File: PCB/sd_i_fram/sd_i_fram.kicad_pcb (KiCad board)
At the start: 2 copper layers, 50 x 40 mm, 11 parts, among them J1 Conn_02x05, J2 Micro_SD_Card

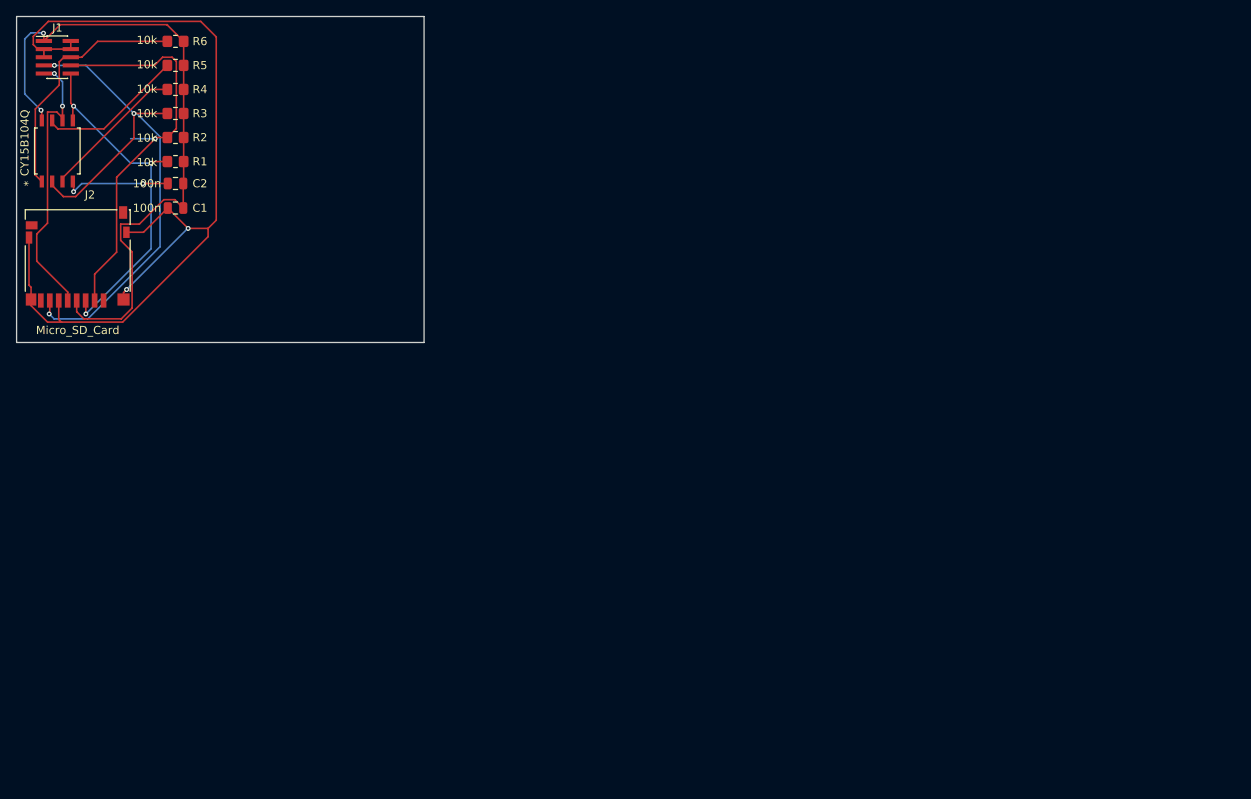
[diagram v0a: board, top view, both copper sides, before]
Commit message: poprawki po 'pracy' michala na schemacie. Poprawione PCB pamieci po Kubie. Grubsze sciezki, poprawiona pozycja decoupling capacitora
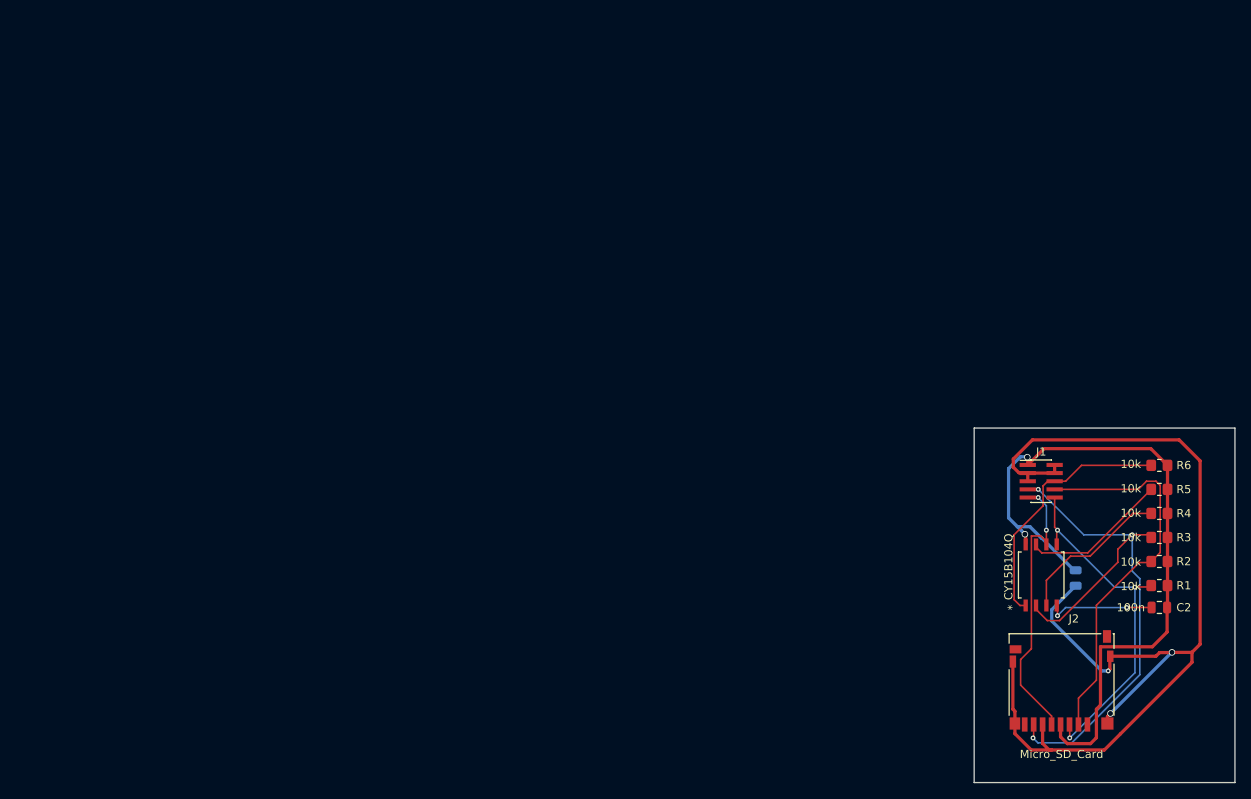
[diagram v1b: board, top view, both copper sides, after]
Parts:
- C1: moved to B.Cu
- moved C2 131.5 mm to (140.2, 72.5)
- moved FRAM1 131.5 mm to (125.7, 68.5)
- moved J1 131.5 mm to (125.7, 57.0)
- moved J2 131.5 mm to (128.2, 81.5)
- moved R1 131.5 mm to (140.2, 69.8)
- moved R2 131.5 mm to (140.2, 66.9)
- moved R3 131.5 mm to (140.2, 63.9)
- moved R4 131.5 mm to (140.2, 61.0)
- moved R5 131.5 mm to (140.2, 58.0)
- moved R6 131.5 mm to (140.2, 55.1)
- moved C1 119.4 mm to (129.9, 68.9), turned to -90 degrees
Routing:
- net /GND_CPU: track 119.2 -> 137.4 mm, vias 2 -> 3
- net /VDD: track 83.1 -> 89.6 mm
- net /SD CS: track 50.9 -> 47.9 mm, vias 1 -> 0
- net Net-(FRAM1-~{WP}): track 17.8 -> 19.3 mm
- net /FRAM CS: track 30.6 -> 31.5 mm
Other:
- board size 50 x 40 mm -> 32 x 43.5 mm
